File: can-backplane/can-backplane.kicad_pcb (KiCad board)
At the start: 4 copper layers, 240 x 70 mm, 61 parts, among them J1 BATT, J10 DSUB-9, J11 DSUB-9, J12 Raspberry_Pi, J13 DSUB-9, J14 DSUB-9, J15 DSUB-9, J16 DSUB-9, J17 DSUB-9, J18 DSUB-9, J19 DSUB-9, J2 DSUB-9, J20 DSUB-9, J21 DSUB-9, J22 DSUB-9, J23 DSUB-9, J3 DSUB-9, J4 DSUB-9, J5 DSUB-9, J6 DSUB-9, J7 DSUB-9, J8 DSUB-9, J9 DSUB-9, U1 TPS566242DRLR, U2 TCAN1044VDDFR, U3 MCP2517FD-xJHA, U4 SN65C3232EDR, Y1 40MHz

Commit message: Cut in  half
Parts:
- removed the J1 at (102.2, 64.2)
- removed J10, J11, J19, J20, J21, J22, J9: DSUB-9, Connector_Dsub:DSUB-9_Female_Vertical_P2.77x2.84mm_MountingHoles
- removed the J18 at (191.1, 98.7)
- removed the J7 at (191.1, 64.9)
- removed the J8 at (206.6, 64.9)
- added J3: 2601-1102, railspeeder:CONN2_2601-1102_WAG, F.Cu at (101.7, 65.0)
- FL1: value Choke -> DLW32SH510XF2L; footprint Inductor_SMD:L_CommonModeChoke_Coilcraft_0603USB -> railspeeder:DLW32PH_MUR
- moved C11 2.80 mm to (69.0, 74.8)
- moved C6 2.80 mm to (69.0, 72.8)
- moved C7 2.80 mm to (69.0, 70.8)
- moved R6 2.80 mm to (66.5, 74.2)
- moved R7 2.80 mm to (66.5, 71.2)
- moved D1 2.80 mm to (71.8, 72.8)
- moved FL1 1.62 mm to (63.0, 72.8), turned to 0 degrees
- renumbered C2 to C1, C22 to C11, C16 to C12, C12 to C13, C8 to C14, C19 to C15, C4 to C16, C9 to C17, C5 to C18, C17 to C19, C14 to C2, C18 to C20, C6 to C21, C20 to C22, C13 to C4, C15 to C5, C1 to C6, C21 to C7, C11 to C8, C7 to C9, J12 to J1, J13 to J14, J14 to J15, J15 to J17, J17 to J18, J23 to J4, J3 to J5, J5 to J6, J4 to J7, J6 to J8, R7 to R1, R6 to R2, R5 to R3, R3 to R5, R1 to R6, R2 to R7, U2 to U1, U3 to U2, U1 to U3
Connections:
- FL1 pad 1: Net-(U2-CANL) -> Net-(U1-CANH)
- FL1 pad 2: /CANL -> /CANH
- FL1 pad 3: /CANH -> /CANL
- FL1 pad 4: Net-(U2-CANH) -> Net-(U1-CANL)
- U1 pad 6: Net-(U2-CANL) -> Net-(U1-CANL)
- U1 pad 7: Net-(U2-CANH) -> Net-(U1-CANH)
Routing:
- net /CANH: track 375.2 -> 218.4 mm
- net /CANL: track 370.2 -> 214.3 mm
- net +3V3: track 69.4 -> 84.0 mm
- net VBUS: track 21.5 -> 26.1 mm
- net Net-(U1-CANL): track 0.00 -> 2.27 mm
- net Net-(U1-CANH): track 0.00 -> 2.19 mm
- net Net-(U2-CANL): track 1.29 -> 0.00 mm
- net Net-(U2-CANH): track 1.29 -> 0.00 mm
- net GND: track 25.6 -> 25.5 mm, vias 29 -> 28
- net +5V: vias 7 -> 8
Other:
- board size 240 x 70 mm -> 165 x 70 mm

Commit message: PCB work for final fab
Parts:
- moved C4 0.23 mm to (51.2, 75.0), turned to 0 degrees
- renumbered C3 to C1, C14 to C10, C15 to C11, C16 to C12, C9 to C13, C17 to C14, C7 to C15, C10 to C16, C11 to C17, C5 to C2, C21 to C20, C20 to C21, C4 to C3, C2 to C4, C1 to C5, C8 to C6, C6 to C7, C12 to C8, C13 to C9, D2 to D1, D1 to D2, J15 to J10, J17 to J11, J16 to J12, J18 to J13, J4 to J2, J2 to J3, J3 to J4, J7 to J6, J6 to J7, J14 to J9, R6 to R5, R5 to R6, U4 to U3, U3 to U4
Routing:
- net Net-(C2-Pad2): track 3.99 -> 5.90 mm
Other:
- board text added: "CAN Backplane UCSC Railspeeder 2025 ::<>"
- board text added: "RS-232"

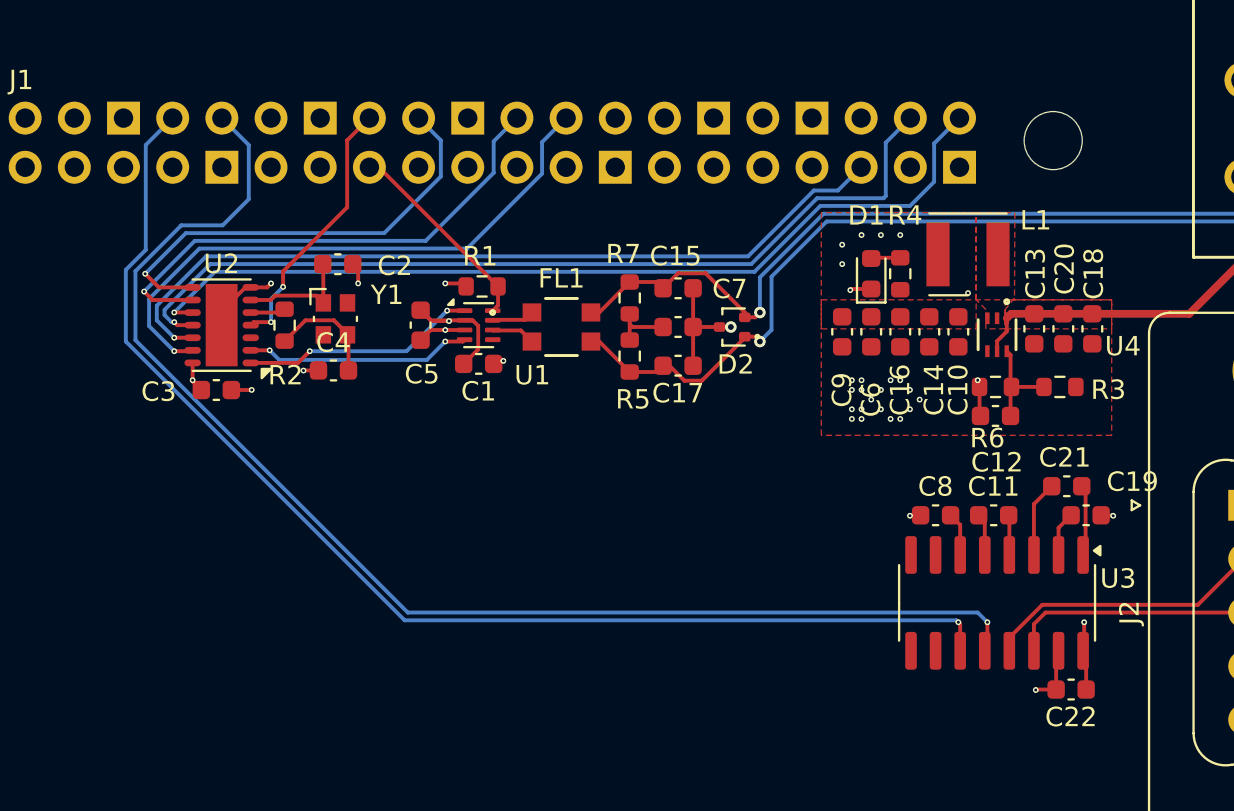
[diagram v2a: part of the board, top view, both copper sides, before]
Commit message: Sweeping via resizing
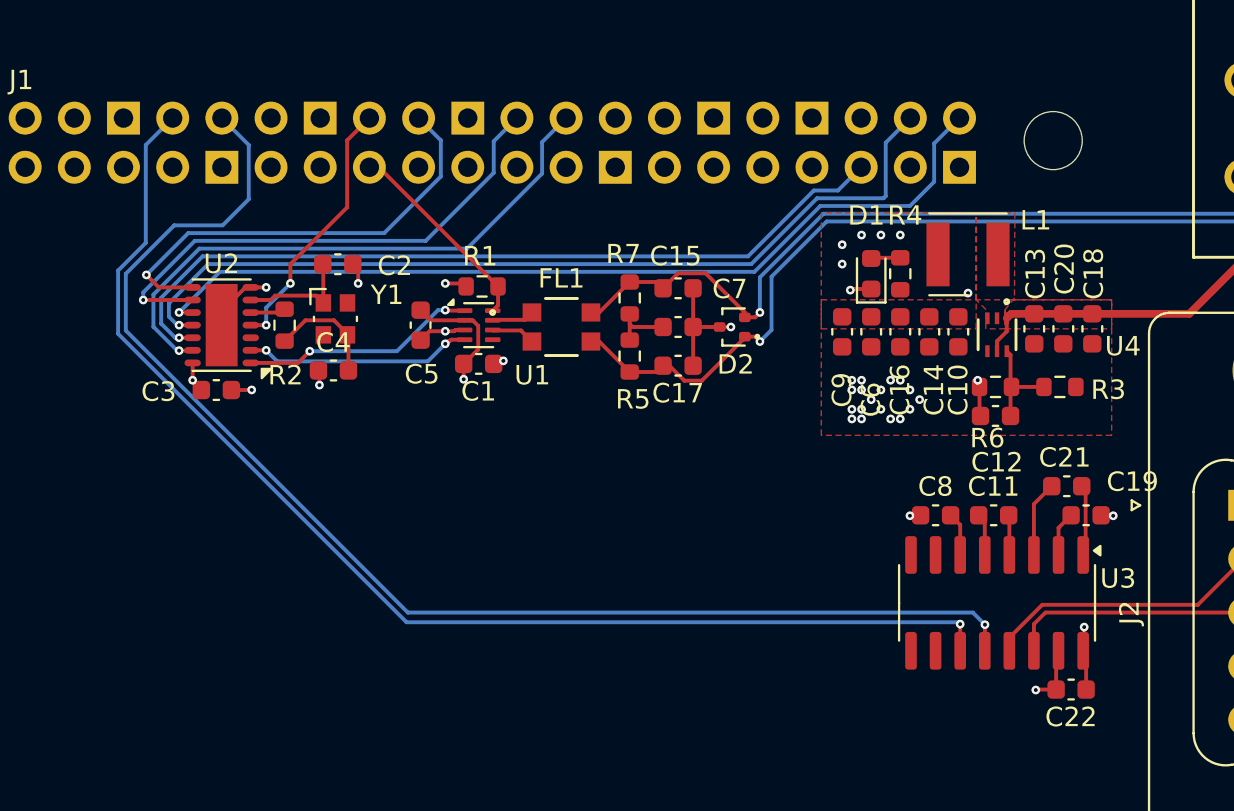
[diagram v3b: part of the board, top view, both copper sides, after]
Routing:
- net GND: track 25.4 -> 24.3 mm
- net +3V3: track 84.0 -> 85.0 mm

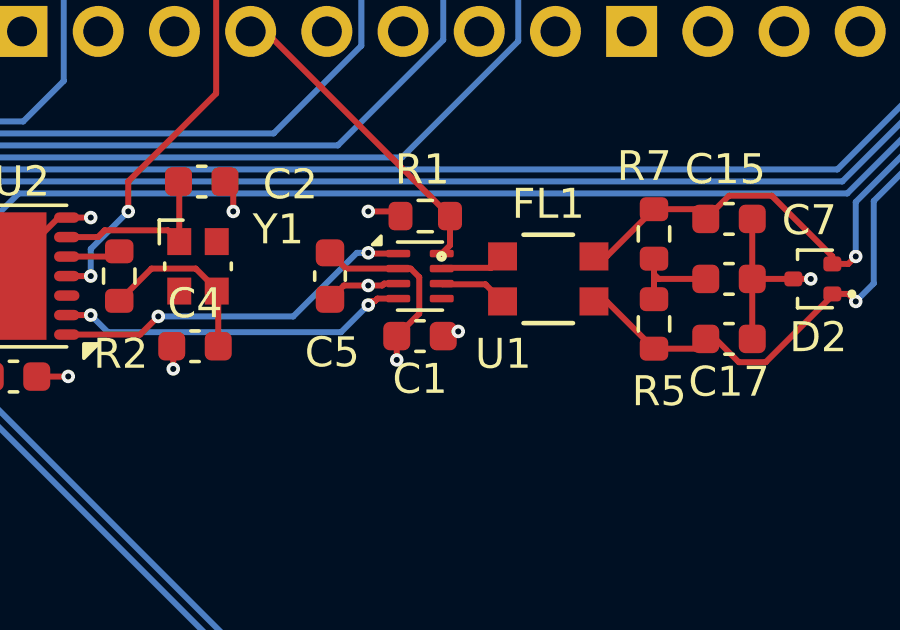
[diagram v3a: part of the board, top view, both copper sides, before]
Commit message: Patched missing trace
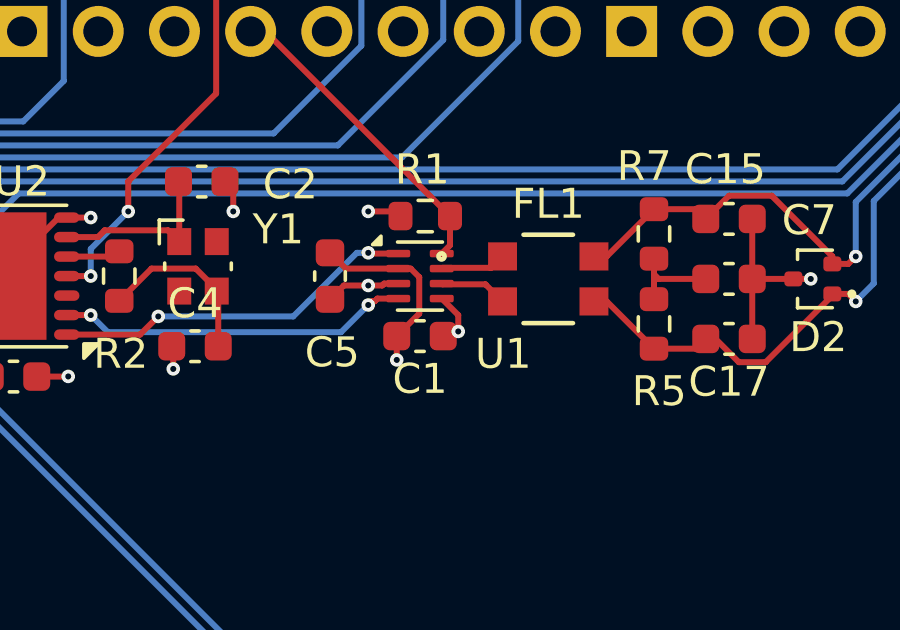
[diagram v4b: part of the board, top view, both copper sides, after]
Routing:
- net +3V3: track 85.0 -> 86.3 mm
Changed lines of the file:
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@@
+	)
+	(segment
+		(start 60 73.955)
+		(end 59.45 73.405)
+		(width 0.2)
+		(layer "F.Cu")
+		(net 4)
+	)
+	(segment
+		(start 60 74.5)
+		(end 60 73.955)
+		(width 0.2)
+		(layer "F.Cu")
+		(net 4)
 	)
 	(segment
